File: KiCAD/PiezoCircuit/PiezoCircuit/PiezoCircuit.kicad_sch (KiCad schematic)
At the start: 10 parts, among them U1 ${SIM.PARAMS}, U2 ${SIM.PARAMS}

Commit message: Cleaning up the documentation
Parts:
- added D4: D_Zener, symbol Device:D_Zener
- added MK2: Piezo, symbol Device:Microphone_Crystal
- added R2, R3: R, symbol Device:R
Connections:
- net GND: now also D4.2 (A), MK2.1 (-), R3.2
- net src_tip: now also D4.1 (K), R2.1, R3.1
- new net: MK2.2 (+), R2.2

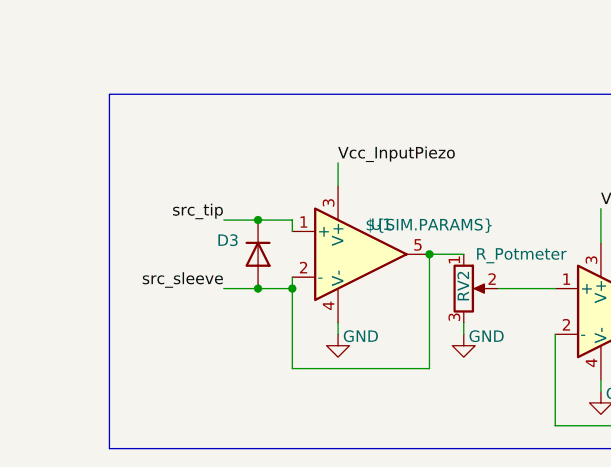
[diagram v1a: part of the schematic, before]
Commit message: Update piezo input circuit
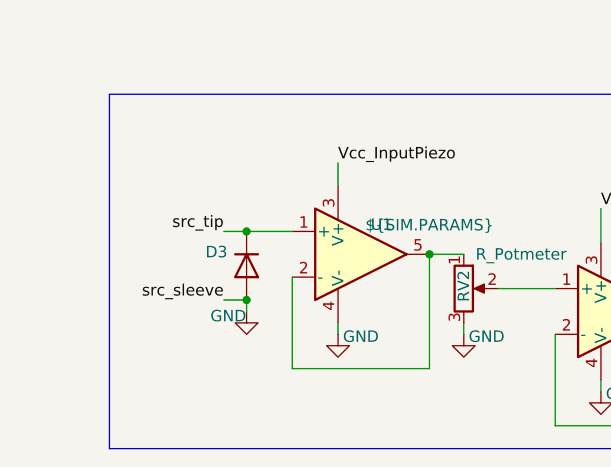
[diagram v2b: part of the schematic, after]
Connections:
- net GND: no longer RV2.1, U1.2 (-), U1.5
- new net: RV2.1, U1.2 (-), U1.5
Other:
- moved on the sheet: D3
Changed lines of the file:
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@@
+	)
+	(junction
+		(at 53.34 116.84)
+		(diameter 0)
+		(color 0 0 0 0)
 	)
 	(junction
@@
 	)
 	(junction
-		(at 54.61 123.19)
+		(at 53.34 124.46)
 		(diameter 0)
 		(color 0 0 0 0)
@@
 	)
 	(junction
-		(at 54.61 115.57)
-		(diameter 0)
-		(color 0 0 0 0)
-	)
-	(junction
-		(at 58.42 123.19)
-		(diameter 0)
-		(color 0 0 0 0)
-	)
-	(junction
 		(at 120.65 36.83)
 		(diameter 0)
@@
 	(wire
 		(pts
-			(xy 54.61 123.19) (xy 58.42 123.19)
-		)
-		(stroke
-			(width 0)
-			(type default)
-		)
-	)
-	(wire
-		(pts
 			(xy 73.66 132.08) (xy 58.42 132.08)
 		)
@@
 	(wire
 		(pts
-			(xy 50.8 115.57) (xy 54.61 115.57)
-		)
-		(stroke
-			(width 0)
-			(type default)
-		)
-	)
-	(wire
-		(pts
-			(xy 54.61 115.57) (xy 58.42 115.57)
-		)
-		(stroke
-			(width 0)
-			(type default)
-		)
-	)
-	(wire
-		(pts
-			(xy 50.8 123.19) (xy 54.61 123.19)
+			(xy 50.8 116.84) (xy 53.34 116.84)
 		)
 		(stroke
@@
 	(wire
 		(pts
+			(xy 53.34 124.46) (xy 53.34 125.73)
+		)
+		(stroke
+			(width 0)
+			(type default)
+		)
+	)
+	(wire
+		(pts
+			(xy 50.8 124.46) (xy 53.34 124.46)
+		)
+		(stroke
+			(width 0)
+			(type default)
+		)
+	)
+	(wire
+		(pts
 			(xy 124.46 69.85) (xy 125.73 69.85)
 		)
@@
 	(wire
 		(pts
-			(xy 58.42 132.08) (xy 58.42 123.19)
-		)
-		(stroke
-			(width 0)
-			(type default)
-		)
-	)
-	(wire
-		(pts
 			(xy 87.63 138.43) (xy 87.63 128.27)
 		)
@@
 	(wire
 		(pts
-			(xy 58.42 123.19) (xy 58.42 121.92)
+			(xy 58.42 121.92) (xy 58.42 132.08)
+		)
+		(stroke
+			(width 0)
+			(type default)
+		)
+	)
+	(wire
+		(pts
+			(xy 53.34 116.84) (xy 58.42 116.84)
 		)
 		(stroke
@@
 		(pts
 			(xy 114.3 46.99) (xy 120.65 46.99)
-		)
-		(stroke
-			(width 0)
-			(type default)
-		)
-	)
-	(wire
-		(pts
-			(xy 58.42 115.57) (xy 58.42 116.84)
 		)
 		(stroke
@@
 	)
 	(label "src_tip"
-		(at 50.8 115.57 180)
+		(at 50.8 116.84 180)
 		(effects
 			(font
@@
 	)
 	(label "src_sleeve"
-		(at 50.8 123.19 180)
+		(at 50.8 124.46 180)
 		(effects
 			(font
@@
 	(symbol
 		(lib_id "Diode:1N4001")
-		(at 54.61 119.38 270)
+		(at 53.34 120.65 270)
 		(unit 1)
 		(exclude_from_sim no)
@@
 		(dnp no)
 		(property "Reference" "D3"
-			(at 50.038 117.856 90)
+			(at 48.768 119.126 90)
 			(effects
 				(font
@@
 		)
 		(property "Value" "~"
-			(at 51.308 119.634 90)
+			(at 50.038 120.904 90)
 			(effects
 				(font
@@
 		)
 		(property "Footprint" "Diode_THT:D_DO-41_SOD81_P10.16mm_Horizontal"
-			(at 54.61 119.38 0)
+			(at 53.34 120.65 0)
 			(effects
 				(font
@@
 		)
 		(property "Datasheet" "http://www.vishay.com/docs/88503/1n4001.pdf"
-			(at 54.61 119.38 0)
+			(at 53.34 120.65 0)
 			(effects
 				(font
@@
 		)
 		(property "Description" "50V 1A General Purpose Rectifier Diode, DO-41"
-			(at 54.61 119.38 0)
+			(at 53.34 120.65 0)
 			(effects
 				(font
@@
 		)
 		(property "Sim.Device" "D"
-			(at 54.61 119.38 0)
+			(at 53.34 120.65 0)
 			(effects
 				(font
@@
 		)
 		(property "Sim.Pins" "1=K 2=A"
-			(at 54.61 119.38 0)
+			(at 53.34 120.65 0)
 			(effects
 				(font
@@
 					(unit 1)
 				)
+			)
+		)
+	)
+	(symbol
+		(lib_id "power:GND")
+		(at 53.34 125.73 0)
+		(unit 1)
+		(exclude_from_sim no)
+		(in_bom yes)
+		(on_board yes)
+		(dnp no)
+		(property "Reference" "#PWR07"
+			(at 53.34 132.08 0)
+			(effects
+				(font
+					(size 1.27 1.27)
+				)
+				(hide yes)
+			)
+		)
+		(property "Value" "GND"
+			(at 51.308 126.238 0)
+			(effects
+				(font
+					(size 1.27 1.27)
+				)
+			)
+		)
+		(property "Footprint" ""
+			(at 53.34 125.73 0)
+			(effects
+				(font
+					(size 1.27 1.27)
+				)
+				(hide yes)
+			)
+		)
+		(property "Datasheet" ""
+			(at 53.34 125.73 0)
+			(effects
+				(font
+					(size 1.27 1.27)
+				)
+				(hide yes)
+			)
+		)
+		(property "Description" "Power symbol creates a global label with name \"GND\" , ground"
+			(at 53.34 125.73 0)
+			(effects
+				(font
+					(size 1.27 1.27)
+				)
+				(hide yes)
+			)
+		)
+		(pin "1"
+		)
+		(instances
+			(project "PiezoCircuit"
+				(path "/e389c290-4bba-4504-9313-1b64e80b2486"
+					(reference "#PWR07")
+					(unit 1)
+				)
